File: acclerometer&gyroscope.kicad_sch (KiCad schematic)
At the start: 5 parts, among them U28 LSM6DS3

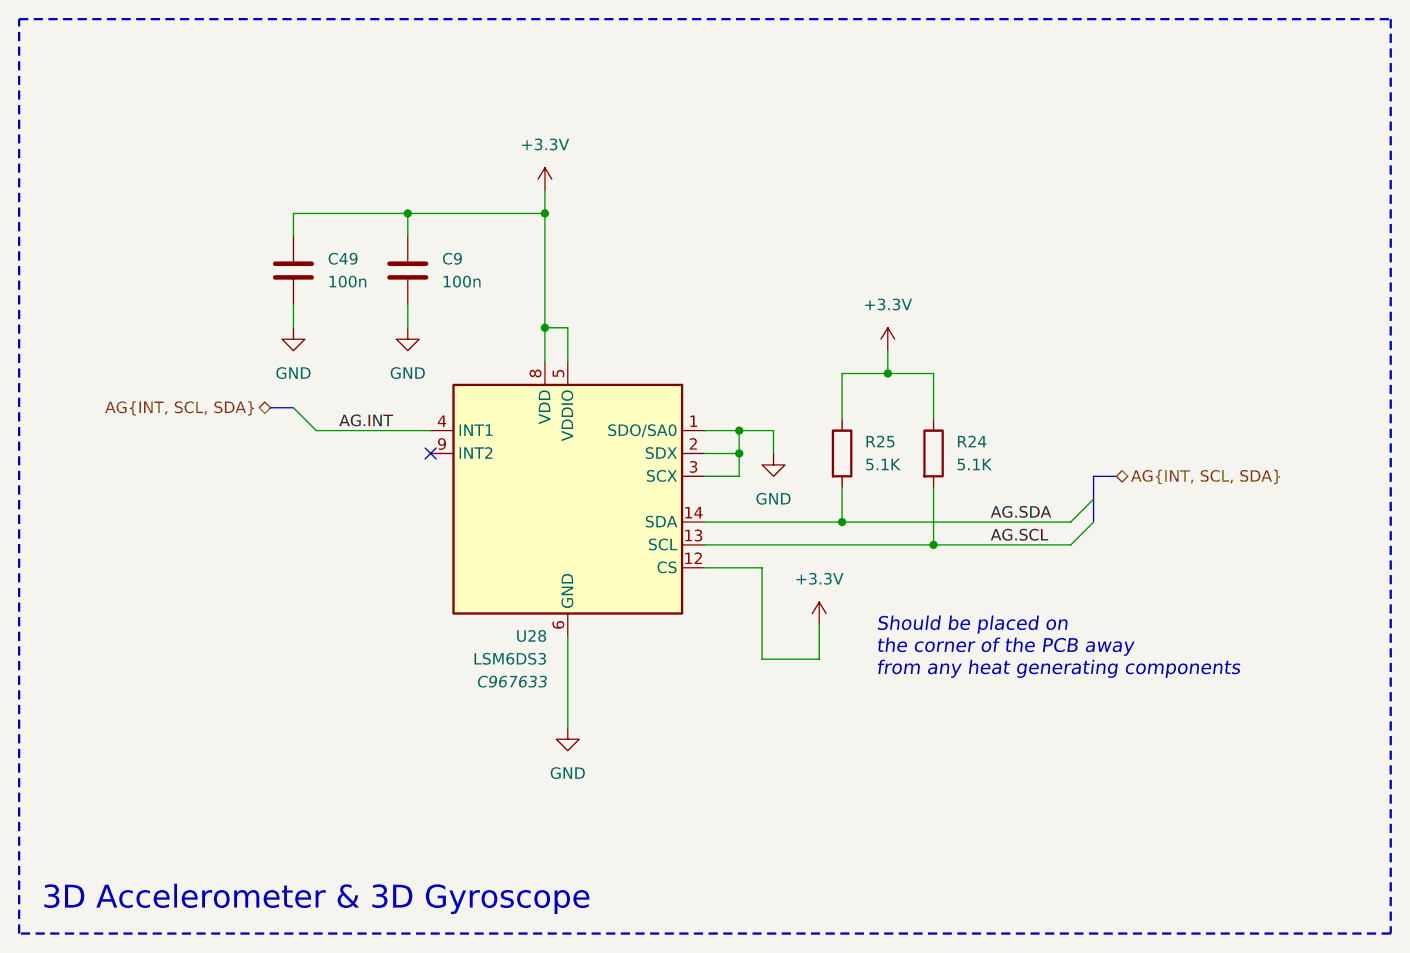
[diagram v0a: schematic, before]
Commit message: PCB routing
- JLCPCB constraints added
- removal of multiple test points
- change of footprints
- change of THT LEDs
- rough position of all the major components
- PCB routing started
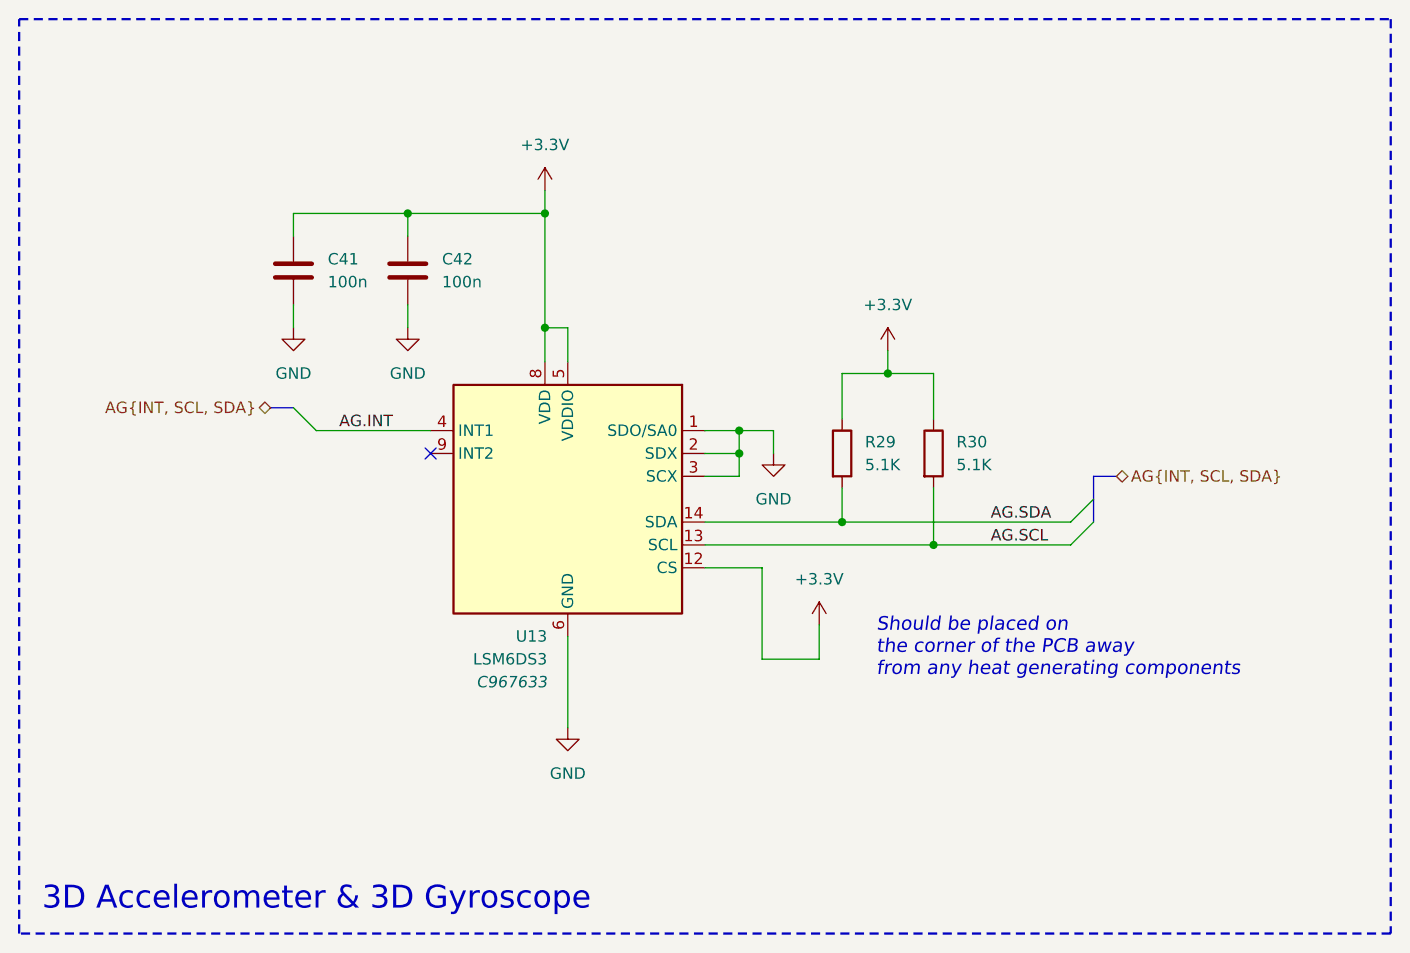
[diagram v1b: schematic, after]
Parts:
- renumbered C49 to C41, C9 to C42, R25 to R29, R24 to R30, U28 to U13
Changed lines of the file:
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@@
 		(dnp no)
 		(fields_autoplaced yes)
-		(property "Reference" "R25"
+		(property "Reference" "R29"
 			(at 163.83 97.7899 0)
 			(effects
@@
 			(project "Precision Clock"
 				(path "/c9a8ff63-a0d1-4125-9dd1-40fb53daf536/83e9a93f-b32e-4175-81a6-6f58261db903"
-					(reference "R25")
+					(reference "R29")
 					(unit 1)
 				)
@@
 		(dnp no)
 		(fields_autoplaced yes)
-		(property "Reference" "R24"
+		(property "Reference" "R30"
 			(at 173.99 97.7899 0)
 			(effects
@@
 			(project "Precision Clock"
 				(path "/c9a8ff63-a0d1-4125-9dd1-40fb53daf536/83e9a93f-b32e-4175-81a6-6f58261db903"
-					(reference "R24")
+					(reference "R30")
 					(unit 1)
 				)
@@
 		(dnp no)
 		(fields_autoplaced yes)
-		(property "Reference" "#PWR026"
+		(property "Reference" "#PWR095"
 			(at 166.37 91.44 0)
 			(effects
@@
 			(project "Precision Clock"
 				(path "/c9a8ff63-a0d1-4125-9dd1-40fb53daf536/83e9a93f-b32e-4175-81a6-6f58261db903"
-					(reference "#PWR026")
+					(reference "#PWR095")
 					(unit 1)
 				)
@@
 		(dnp no)
 		(fields_autoplaced yes)
-		(property "Reference" "#PWR022"
+		(property "Reference" "#PWR091"
 			(at 128.27 73.66 0)
 			(effects
@@
 			(project "Precision Clock"
 				(path "/c9a8ff63-a0d1-4125-9dd1-40fb53daf536/83e9a93f-b32e-4175-81a6-6f58261db903"
-					(reference "#PWR022")
+					(reference "#PWR091")
 					(unit 1)
 				)
@@
 		(on_board yes)
 		(dnp no)
-		(property "Reference" "U28"
+		(property "Reference" "U13"
 			(at 128.524 119.38 0)
 			(effects
@@
 			(project "Precision Clock"
 				(path "/c9a8ff63-a0d1-4125-9dd1-40fb53daf536/83e9a93f-b32e-4175-81a6-6f58261db903"
-					(reference "U28")
+					(reference "U13")
 					(unit 1)
 				)
@@
 		(dnp no)
 		(fields_autoplaced yes)
-		(property "Reference" "C9"
+		(property "Reference" "C42"
 			(at 116.84 77.4699 0)
 			(effects
@@
 			(project "Precision Clock"
 				(path "/c9a8ff63-a0d1-4125-9dd1-40fb53daf536/83e9a93f-b32e-4175-81a6-6f58261db903"
-					(reference "C9")
+					(reference "C42")
 					(unit 1)
 				)
@@
 		(dnp no)
 		(fields_autoplaced yes)
-		(property "Reference" "#PWR021"
+		(property "Reference" "#PWR090"
 			(at 113.03 91.44 0)
 			(effects
@@
 			(project "Precision Clock"
 				(path "/c9a8ff63-a0d1-4125-9dd1-40fb53daf536/83e9a93f-b32e-4175-81a6-6f58261db903"
-					(reference "#PWR021")
+					(reference "#PWR090")
 					(unit 1)
 				)
@@
 		(dnp no)
 		(fields_autoplaced yes)
-		(property "Reference" "#PWR025"
+		(property "Reference" "#PWR094"
 			(at 158.75 121.92 0)
 			(effects
@@
 			(project "Precision Clock"
 				(path "/c9a8ff63-a0d1-4125-9dd1-40fb53daf536/83e9a93f-b32e-4175-81a6-6f58261db903"
-					(reference "#PWR025")
+					(reference "#PWR094")
 					(unit 1)
 				)
@@
 		(dnp no)
 		(fields_autoplaced yes)
-		(property "Reference" "C49"
+		(property "Reference" "C41"
 			(at 104.14 77.4699 0)
 			(effects
@@
 			(project "Precision Clock"
 				(path "/c9a8ff63-a0d1-4125-9dd1-40fb53daf536/83e9a93f-b32e-4175-81a6-6f58261db903"
-					(reference "C49")
+					(reference "C41")
 					(unit 1)
 				)
@@
 		(dnp no)
 		(fields_autoplaced yes)
-		(property "Reference" "#PWR0115"
+		(property "Reference" "#PWR089"
 			(at 100.33 91.44 0)
 			(effects
@@
 			(project "Precision Clock"
 				(path "/c9a8ff63-a0d1-4125-9dd1-40fb53daf536/83e9a93f-b32e-4175-81a6-6f58261db903"
-					(reference "#PWR0115")
+					(reference "#PWR089")
 					(unit 1)
 				)
@@
 		(dnp no)
 		(fields_autoplaced yes)
-		(property "Reference" "#PWR023"
+		(property "Reference" "#PWR092"
 			(at 130.81 135.89 0)
 			(effects
@@
 			(project "Precision Clock"
 				(path "/c9a8ff63-a0d1-4125-9dd1-40fb53daf536/83e9a93f-b32e-4175-81a6-6f58261db903"
-					(reference "#PWR023")
+					(reference "#PWR092")
 					(unit 1)
 				)
@@
 		(dnp no)
 		(fields_autoplaced yes)
-		(property "Reference" "#PWR024"
+		(property "Reference" "#PWR093"
 			(at 153.67 105.41 0)
 			(effects
@@
 			(project "Precision Clock"
 				(path "/c9a8ff63-a0d1-4125-9dd1-40fb53daf536/83e9a93f-b32e-4175-81a6-6f58261db903"
-					(reference "#PWR024")
-					(unit 1)
-				)
+					(reference "#PWR093")
+					(unit 1)
+				)

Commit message: PCB routing
- addition of 3D models
- addition of docs
- reduction of the size of passives
- increase in size of traces
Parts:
- C41, C42: footprint Capacitor_SMD:C_0603_1608Metric -> Capacitor_SMD:C_0402_1005Metric
- R29, R30: footprint Resistor_SMD:R_0603_1608Metric -> Resistor_SMD:R_0402_1005Metric
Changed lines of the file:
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@@
 			)
 		)
-		(property "Footprint" "Resistor_SMD:R_0603_1608Metric"
+		(property "Footprint" "Resistor_SMD:R_0402_1005Metric"
 			(at 159.512 99.06 90)
 			(effects
@@
 			)
 		)
-		(property "Footprint" "Resistor_SMD:R_0603_1608Metric"
+		(property "Footprint" "Resistor_SMD:R_0402_1005Metric"
 			(at 169.672 99.06 90)
 			(effects
@@
 			)
 		)
-		(property "Footprint" "Capacitor_SMD:C_0603_1608Metric"
+		(property "Footprint" "Capacitor_SMD:C_0402_1005Metric"
 			(at 112.0648 82.55 0)
 			(effects
@@
 			)
 		)
-		(property "Footprint" "Capacitor_SMD:C_0603_1608Metric"
+		(property "Footprint" "Capacitor_SMD:C_0402_1005Metric"
 			(at 99.3648 82.55 0)
 			(effects

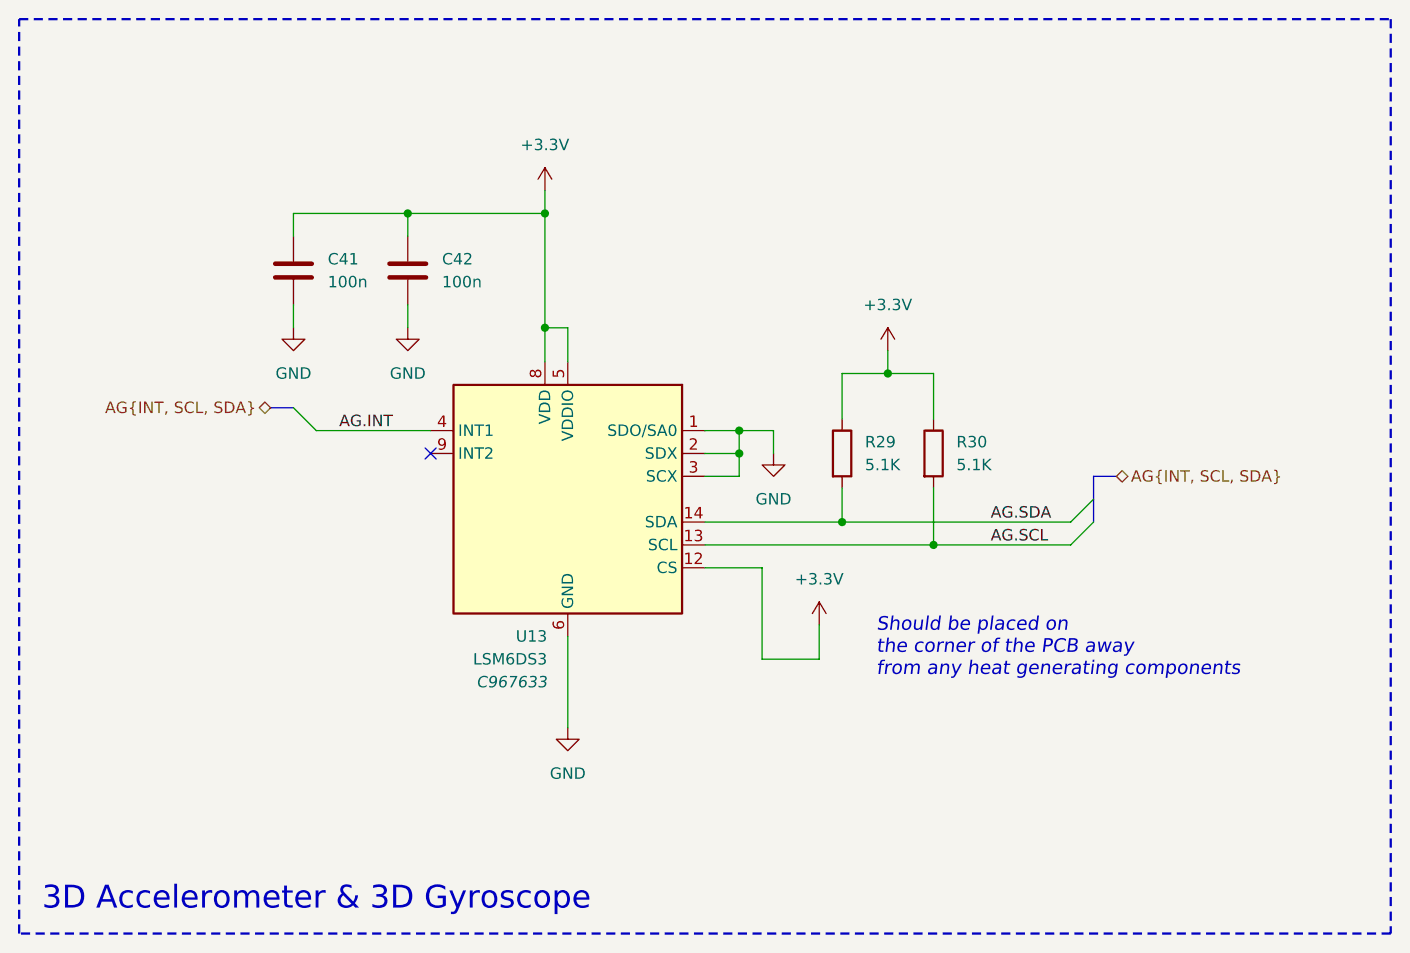
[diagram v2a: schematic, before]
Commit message: Primary MCU rerouting
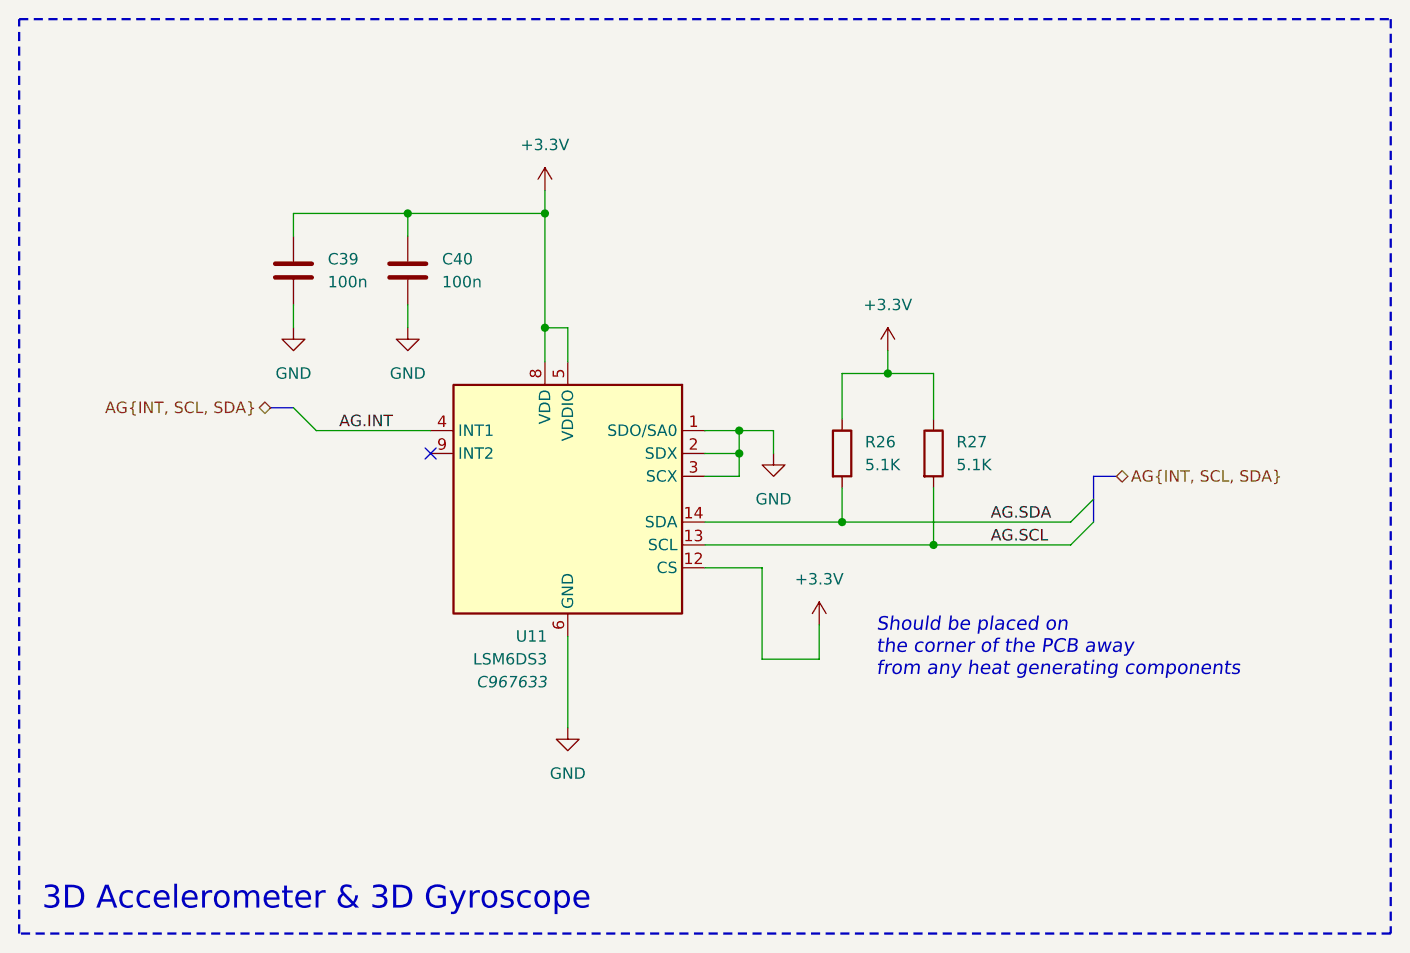
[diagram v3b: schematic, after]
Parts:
- renumbered C41 to C39, C42 to C40, R29 to R26, R30 to R27, U13 to U11
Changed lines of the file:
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@@
 		(dnp no)
 		(fields_autoplaced yes)
-		(property "Reference" "R29"
+		(property "Reference" "R26"
 			(at 163.83 97.7899 0)
 			(effects
@@
 			(project "Precision Clock"
 				(path "/c9a8ff63-a0d1-4125-9dd1-40fb53daf536/83e9a93f-b32e-4175-81a6-6f58261db903"
-					(reference "R29")
+					(reference "R26")
 					(unit 1)
 				)
@@
 		(dnp no)
 		(fields_autoplaced yes)
-		(property "Reference" "R30"
+		(property "Reference" "R27"
 			(at 173.99 97.7899 0)
 			(effects
@@
 			(project "Precision Clock"
 				(path "/c9a8ff63-a0d1-4125-9dd1-40fb53daf536/83e9a93f-b32e-4175-81a6-6f58261db903"
-					(reference "R30")
+					(reference "R27")
 					(unit 1)
 				)
@@
 		(dnp no)
 		(fields_autoplaced yes)
-		(property "Reference" "#PWR095"
+		(property "Reference" "#PWR087"
 			(at 166.37 91.44 0)
 			(effects
@@
 			(project "Precision Clock"
 				(path "/c9a8ff63-a0d1-4125-9dd1-40fb53daf536/83e9a93f-b32e-4175-81a6-6f58261db903"
-					(reference "#PWR095")
+					(reference "#PWR087")
 					(unit 1)
 				)
@@
 		(dnp no)
 		(fields_autoplaced yes)
-		(property "Reference" "#PWR091"
+		(property "Reference" "#PWR083"
 			(at 128.27 73.66 0)
 			(effects
@@
 			(project "Precision Clock"
 				(path "/c9a8ff63-a0d1-4125-9dd1-40fb53daf536/83e9a93f-b32e-4175-81a6-6f58261db903"
-					(reference "#PWR091")
+					(reference "#PWR083")
 					(unit 1)
 				)
@@
 		(on_board yes)
 		(dnp no)
-		(property "Reference" "U13"
+		(property "Reference" "U11"
 			(at 128.524 119.38 0)
 			(effects
@@
 			(project "Precision Clock"
 				(path "/c9a8ff63-a0d1-4125-9dd1-40fb53daf536/83e9a93f-b32e-4175-81a6-6f58261db903"
-					(reference "U13")
+					(reference "U11")
 					(unit 1)
 				)
@@
 		(dnp no)
 		(fields_autoplaced yes)
-		(property "Reference" "C42"
+		(property "Reference" "C40"
 			(at 116.84 77.4699 0)
 			(effects
@@
 			(project "Precision Clock"
 				(path "/c9a8ff63-a0d1-4125-9dd1-40fb53daf536/83e9a93f-b32e-4175-81a6-6f58261db903"
-					(reference "C42")
+					(reference "C40")
 					(unit 1)
 				)
@@
 		(dnp no)
 		(fields_autoplaced yes)
-		(property "Reference" "#PWR090"
+		(property "Reference" "#PWR082"
 			(at 113.03 91.44 0)
 			(effects
@@
 			(project "Precision Clock"
 				(path "/c9a8ff63-a0d1-4125-9dd1-40fb53daf536/83e9a93f-b32e-4175-81a6-6f58261db903"
-					(reference "#PWR090")
+					(reference "#PWR082")
 					(unit 1)
 				)
@@
 		(dnp no)
 		(fields_autoplaced yes)
-		(property "Reference" "#PWR094"
+		(property "Reference" "#PWR086"
 			(at 158.75 121.92 0)
 			(effects
@@
 			(project "Precision Clock"
 				(path "/c9a8ff63-a0d1-4125-9dd1-40fb53daf536/83e9a93f-b32e-4175-81a6-6f58261db903"
-					(reference "#PWR094")
+					(reference "#PWR086")
 					(unit 1)
 				)
@@
 		(dnp no)
 		(fields_autoplaced yes)
-		(property "Reference" "C41"
+		(property "Reference" "C39"
 			(at 104.14 77.4699 0)
 			(effects
@@
 			(project "Precision Clock"
 				(path "/c9a8ff63-a0d1-4125-9dd1-40fb53daf536/83e9a93f-b32e-4175-81a6-6f58261db903"
-					(reference "C41")
+					(reference "C39")
 					(unit 1)
 				)
@@
 		(dnp no)
 		(fields_autoplaced yes)
-		(property "Reference" "#PWR089"
+		(property "Reference" "#PWR081"
 			(at 100.33 91.44 0)
 			(effects
@@
 			(project "Precision Clock"
 				(path "/c9a8ff63-a0d1-4125-9dd1-40fb53daf536/83e9a93f-b32e-4175-81a6-6f58261db903"
-					(reference "#PWR089")
+					(reference "#PWR081")
 					(unit 1)
 				)
@@
 		(dnp no)
 		(fields_autoplaced yes)
-		(property "Reference" "#PWR092"
+		(property "Reference" "#PWR084"
 			(at 130.81 135.89 0)
 			(effects
@@
 			(project "Precision Clock"
 				(path "/c9a8ff63-a0d1-4125-9dd1-40fb53daf536/83e9a93f-b32e-4175-81a6-6f58261db903"
-					(reference "#PWR092")
+					(reference "#PWR084")
 					(unit 1)
 				)
@@
 		(dnp no)
 		(fields_autoplaced yes)
-		(property "Reference" "#PWR093"
+		(property "Reference" "#PWR085"
 			(at 153.67 105.41 0)
 			(effects
@@
 			(project "Precision Clock"
 				(path "/c9a8ff63-a0d1-4125-9dd1-40fb53daf536/83e9a93f-b32e-4175-81a6-6f58261db903"
-					(reference "#PWR093")
-					(unit 1)
-				)
+					(reference "#PWR085")
+					(unit 1)
+				)
